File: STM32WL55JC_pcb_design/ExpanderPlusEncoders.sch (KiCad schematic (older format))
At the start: 8 parts

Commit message: Update ADC section to work with MAX11635
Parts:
- removed J? (x4): Conn_01x10_Male, Connector_JST:JST_GH_BM10B-GHS-TBT_1x10-1MP_P1.25mm_Vertical, symbol Connector:Conn_01x10_Male
- removed R?: 4k7, symbol Device:R_US
- added J? (x4): Conn_01x10, Connector_JST:JST_GH_BM10B-GHS-TBT_1x10-1MP_P1.25mm_Vertical, symbol Connector_Generic:Conn_01x10
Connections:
- wire segments 50 -> 46
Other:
- moved on the sheet: SW?
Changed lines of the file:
@@
 $Descr A4 11693 8268
 encoding utf-8
-Sheet 5 6
+Sheet 2 6
 Title ""
 Date ""
@@
 Wire Wire Line
 	2850 3300 2950 3300
-$Comp
-L Connector:Conn_01x10_Male J?
-U 1 1 6179BFE6
-P 2650 2900
-AR Path="/6179BFE6" Ref="J?"  Part="1"
-AR Path="/61789BD1/6179BFE6" Ref="J?"  Part="1"
-F 0 "J?" H 2758 3481 50  0000 C CNN
-F 1 "Conn_01x10_Male" H 2758 3390 50  0000 C CNN
-F 2 "Connector_JST:JST_GH_BM10B-GHS-TBT_1x10-1MP_P1.25mm_Vertical" H 2650 2900 50  0001 C CNN
-F 3 "~" H 2650 2900 50  0001 C CNN
-	1    2650 2900
-	1    0    0    -1
-$EndComp
 Text GLabel 2950 2500 2    50   Input ~ 0
 ENC1_1
@@
 Wire Wire Line
 	3800 3300 3900 3300
-$Comp
-L Connector:Conn_01x10_Male J?
-U 1 1 6179C000
-P 3600 2900
-AR Path="/6179C000" Ref="J?"  Part="1"
-AR Path="/61789BD1/6179C000" Ref="J?"  Part="1"
-F 0 "J?" H 3708 3481 50  0000 C CNN
-F 1 "Conn_01x10_Male" H 3708 3390 50  0000 C CNN
-F 2 "Connector_JST:JST_GH_BM10B-GHS-TBT_1x10-1MP_P1.25mm_Vertical" H 3600 2900 50  0001 C CNN
-F 3 "~" H 3600 2900 50  0001 C CNN
-	1    3600 2900
-	1    0    0    -1
-$EndComp
 Text GLabel 3900 2500 2    50   Input ~ 0
 ENC3_1
@@
 Wire Wire Line
 	2850 4500 2950 4500
-$Comp
-L Connector:Conn_01x10_Male J?
-U 1 1 6179C019
-P 2650 4100
-AR Path="/6179C019" Ref="J?"  Part="1"
-AR Path="/61789BD1/6179C019" Ref="J?"  Part="1"
-F 0 "J?" H 2758 4681 50  0000 C CNN
-F 1 "Conn_01x10_Male" H 2758 4590 50  0000 C CNN
-F 2 "Connector_JST:JST_GH_BM10B-GHS-TBT_1x10-1MP_P1.25mm_Vertical" H 2650 4100 50  0001 C CNN
-F 3 "~" H 2650 4100 50  0001 C CNN
-	1    2650 4100
-	1    0    0    -1
-$EndComp
 Text GLabel 2950 3700 2    50   Input ~ 0
 ENC5_1
@@
 Wire Wire Line
 	3800 4500 3900 4500
-$Comp
-L Connector:Conn_01x10_Male J?
-U 1 1 6179C032
-P 3600 4100
-AR Path="/6179C032" Ref="J?"  Part="1"
-AR Path="/61789BD1/6179C032" Ref="J?"  Part="1"
-F 0 "J?" H 3708 4681 50  0000 C CNN
-F 1 "Conn_01x10_Male" H 3708 4590 50  0000 C CNN
-F 2 "Connector_JST:JST_GH_BM10B-GHS-TBT_1x10-1MP_P1.25mm_Vertical" H 3600 4100 50  0001 C CNN
-F 3 "~" H 3600 4100 50  0001 C CNN
-	1    3600 4100
-	1    0    0    -1
-$EndComp
 Text GLabel 3900 3700 2    50   Input ~ 0
 ENC7_1
@@
 Text HLabel 8500 2400 2    50   Input ~ 0
 EXP_VDD
-Wire Wire Line
-	8500 3700 8900 3700
 $Comp
 L Switch:SW_MEC_5E SW?
 U 1 1 617D8DFE
-P 9100 3800
-F 0 "SW?" H 9100 4185 50  0000 C CNN
-F 1 "SW_MEC_5E" H 9100 4094 50  0000 C CNN
-F 2 "" H 9100 4100 50  0001 C CNN
-F 3 "http://www.apem.com/int/index.php?controller=attachment&id_attachment=1371" H 9100 4100 50  0001 C CNN
-	1    9100 3800
+P 9300 3800
+F 0 "SW?" H 9300 4185 50  0000 C CNN
+F 1 "SW_MEC_5E" H 9300 4094 50  0000 C CNN
+F 2 "" H 9300 4100 50  0001 C CNN
+F 3 "http://www.apem.com/int/index.php?controller=attachment&id_attachment=1371" H 9300 4100 50  0001 C CNN
+	1    9300 3800
 	1    0    0    -1
 $EndComp
-Wire Wire Line
-	8900 3700 8900 3800
-Connection ~ 8900 3700
-Wire Wire Line
-	9300 3800 9300 3700
-Text HLabel 9350 3800 2    50   Input ~ 0
-EXP_GND
-Text HLabel 9250 4600 2    50   Input ~ 0
+Text HLabel 8500 4600 2    50   Input ~ 0
 EXP_INT
-$Comp
-L Device:R_US R?
-U 1 1 617DE762
-P 9050 4450
-F 0 "R?" H 9118 4496 50  0000 L CNN
-F 1 "4k7" H 9118 4405 50  0000 L CNN
-F 2 "" V 9090 4440 50  0001 C CNN
-F 3 "~" H 9050 4450 50  0001 C CNN
-	1    9050 4450
-	1    0    0    -1
-$EndComp
-Wire Wire Line
-	9050 4300 9050 4200
-Wire Wire Line
-	9050 4600 9250 4600
-Wire Wire Line
-	9050 4600 8500 4600
-Connection ~ 9050 4600
-Wire Wire Line
-	9050 4200 9100 4200
-Wire Wire Line
-	9300 3800 9350 3800
-Connection ~ 9300 3800
-Text HLabel 9100 4200 2    50   Input ~ 0
-EXP_VDD
 Text HLabel 2950 3300 2    50   Input ~ 0
 OR1
@@
 Text GLabel 5700 4200 0    50   Input ~ 0
 ENC_RST_4
+Text HLabel 9750 3700 2    50   Input ~ 0
+EXP_VDD
+Wire Wire Line
+	9500 3700 9750 3700
+Wire Wire Line
+	8500 3700 9100 3700
+Wire Wire Line
+	9100 3700 9100 3800
+Connection ~ 9100 3700
+Wire Wire Line
+	9500 3700 9500 3800
+Connection ~ 9500 3700
+$Comp
+L Connector_Generic:Conn_01x10 J?
+U 1 1 61681B58
+P 2650 3000
+F 0 "J?" H 2568 2275 50  0000 C CNN
+F 1 "Conn_01x10" H 2568 2366 50  0000 C CNN
+F 2 "Connector_JST:JST_GH_BM10B-GHS-TBT_1x10-1MP_P1.25mm_Vertical" H 2650 3000 50  0001 C CNN
+F 3 "~" H 2650 3000 50  0001 C CNN
+	1    2650 3000
+	-1   0    0    1
+$EndComp
+$Comp
+L Connector_Generic:Conn_01x10 J?
+U 1 1 6168626C
+P 3600 3000
+F 0 "J?" H 3518 2275 50  0000 C CNN
+F 1 "Conn_01x10" H 3518 2366 50  0000 C CNN
+F 2 "Connector_JST:JST_GH_BM10B-GHS-TBT_1x10-1MP_P1.25mm_Vertical" H 3600 3000 50  0001 C CNN
+F 3 "~" H 3600 3000 50  0001 C CNN
+	1    3600 3000
+	-1   0    0    1
+$EndComp
+$Comp
+L Connector_Generic:Conn_01x10 J?
+U 1 1 61686F2D
+P 2650 4200
+F 0 "J?" H 2568 3475 50  0000 C CNN
+F 1 "Conn_01x10" H 2568 3566 50  0000 C CNN
+F 2 "Connector_JST:JST_GH_BM10B-GHS-TBT_1x10-1MP_P1.25mm_Vertical" H 2650 4200 50  0001 C CNN
+F 3 "~" H 2650 4200 50  0001 C CNN
+	1    2650 4200
+	-1   0    0    1
+$EndComp
+$Comp
+L Connector_Generic:Conn_01x10 J?
+U 1 1 61688106
+P 3600 4200
+F 0 "J?" H 3518 3475 50  0000 C CNN
+F 1 "Conn_01x10" H 3518 3566 50  0000 C CNN
+F 2 "Connector_JST:JST_GH_BM10B-GHS-TBT_1x10-1MP_P1.25mm_Vertical" H 3600 4200 50  0001 C CNN
+F 3 "~" H 3600 4200 50  0001 C CNN
+	1    3600 4200
+	-1   0    0    1
+$EndComp
 $EndSCHEMATC

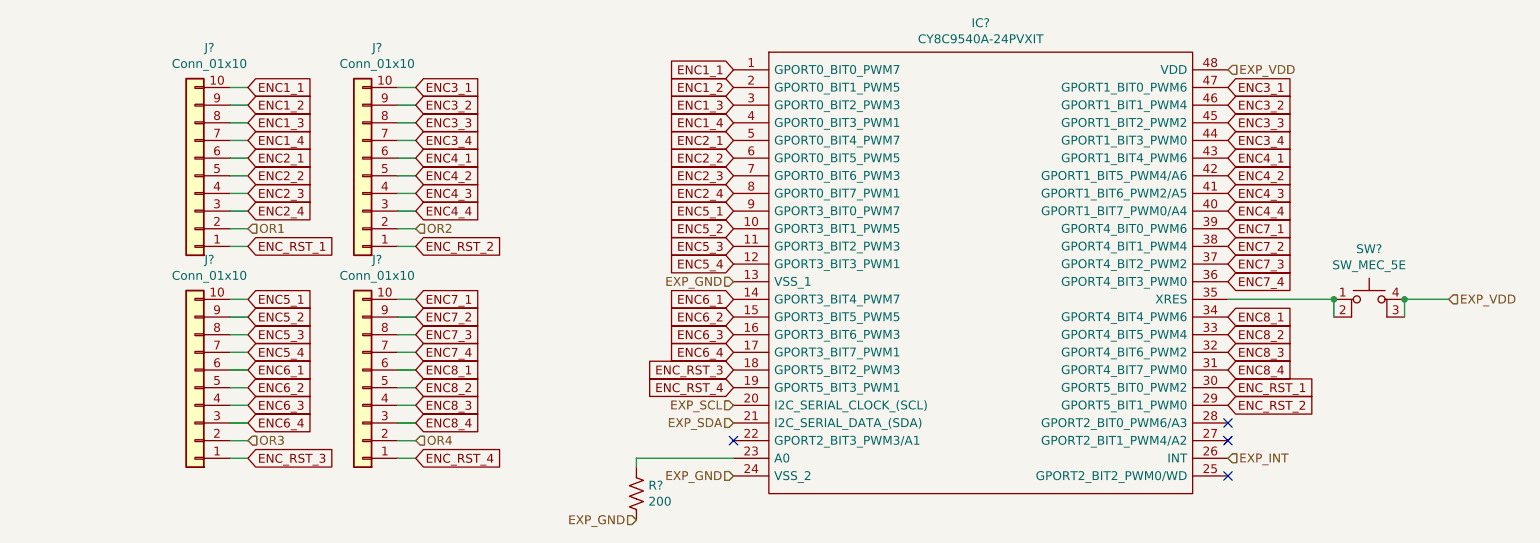
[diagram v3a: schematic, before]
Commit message: Finish component selection and footprint assignment
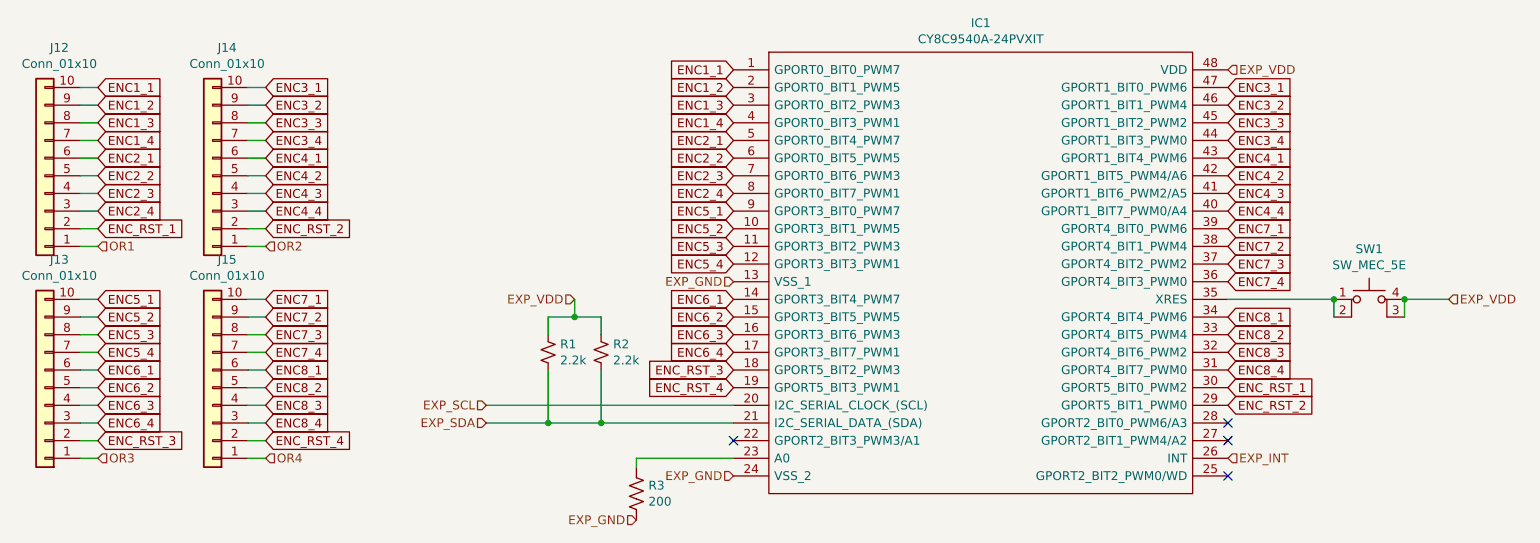
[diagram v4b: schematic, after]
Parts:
- added R1, R2: 2.2k, Resistor_SMD:R_0805_2012Metric, symbol Device:R_Small_US
- IC1: renamed from IC?; footprint SOP64P1035X279-48N -> CY8C9540A-24PVXIT:SOP64P1035X279-48N
- R3: renamed from R?; footprint (none) -> Resistor_SMD:R_0805_2012Metric
- SW1: renamed from SW?; footprint (none) -> EVQ-P2F02K:EVQP2V02W
- gave numbers to parts that had none: 4
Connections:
- net ENC_RST_1: now also J12.2 (Pin_2); no longer J12.1 (Pin_1)
- net ENC_RST_2: now also J14.2 (Pin_2); no longer J14.1 (Pin_1)
- net ENC_RST_3: now also J13.2 (Pin_2); no longer J13.1 (Pin_1)
- net ENC_RST_4: now also J15.2 (Pin_2); no longer J15.1 (Pin_1)
- net EXP_SDA: now also R1.2, R2.2
- net EXP_VDD: now also R1.1, R2.1
- net OR1: now also J12.1 (Pin_1); no longer J12.2 (Pin_2)
- net OR2: now also J14.1 (Pin_1); no longer J14.2 (Pin_2)
- net OR3: now also J13.1 (Pin_1); no longer J13.2 (Pin_2)
- net OR4: now also J15.1 (Pin_1); no longer J15.2 (Pin_2)
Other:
- moved on the sheet: J12, J13, J14, J15

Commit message: Initial pcb layout
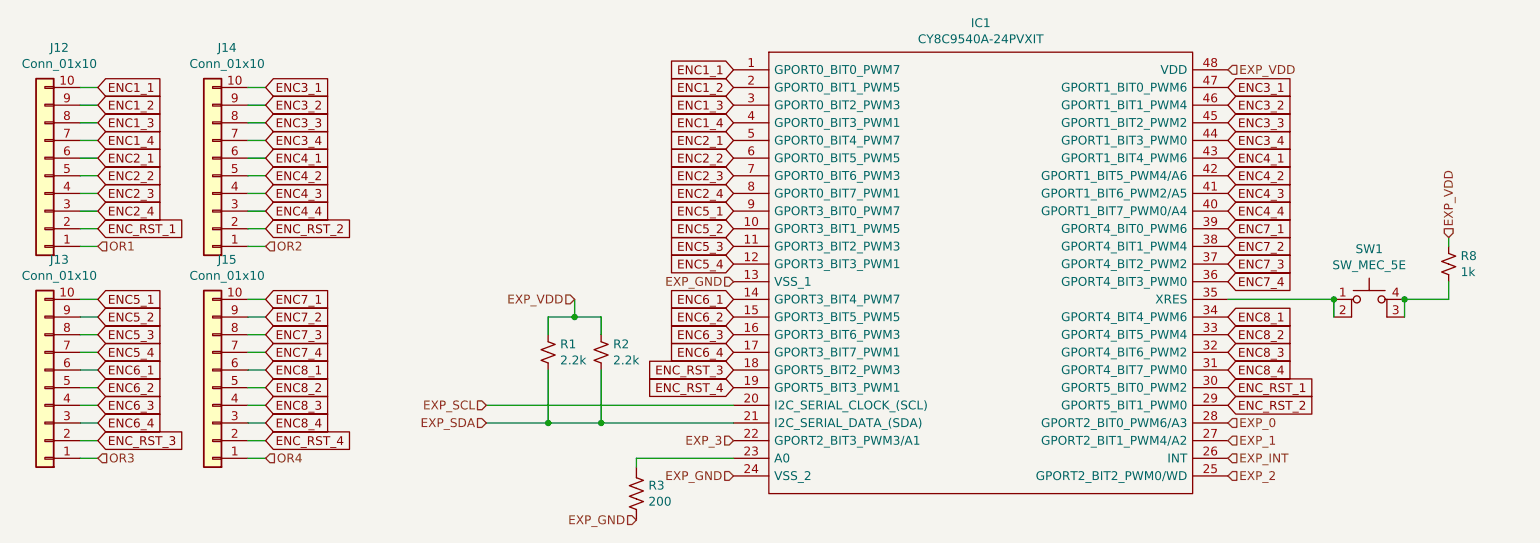
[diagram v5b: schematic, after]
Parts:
- added R8: 1k, Resistor_SMD:R_0805_2012Metric, symbol Device:R_Small_US
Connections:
- net EXP_VDD: now also R8.1; no longer SW1.3 (K), SW1.4 (A)
- net EXP_3: now reaches IC1.22 (GPORT2_BIT3_PWM3/A1)
- net EXP_2: now reaches IC1.25 (GPORT2_BIT2_PWM0/WD)
- net EXP_1: now reaches IC1.27 (GPORT2_BIT1_PWM4/A2)
- net EXP_0: now reaches IC1.28 (GPORT2_BIT0_PWM6/A3)
- new net: R8.2, SW1.3 (K), SW1.4 (A)
- no-connect marks 4 -> 0
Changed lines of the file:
@@
 Text HLabel 5150 4950 0    50   Input ~ 0
 EXP_GND
-NoConn ~ 5700 4500
-NoConn ~ 8500 4400
-NoConn ~ 8500 4500
-NoConn ~ 8500 4700
 Text GLabel 2100 3300 2    50   Input ~ 0
 ENC_RST_1
@@
 Text GLabel 5700 4200 0    50   Input ~ 0
 ENC_RST_4
-Text HLabel 9750 3700 2    50   Input ~ 0
+Text HLabel 9750 3350 1    50   Input ~ 0
 EXP_VDD
 Wire Wire Line
@@
 Text HLabel 4800 3700 0    50   Input ~ 0
 EXP_VDD
+$Comp
+L Device:R_Small_US R8
+U 1 1 615EB589
+P 9750 3500
+F 0 "R8" H 9818 3546 50  0000 L CNN
+F 1 "1k" H 9818 3455 50  0000 L CNN
+F 2 "Resistor_SMD:R_0805_2012Metric" H 9750 3500 50  0001 C CNN
+F 3 "~" H 9750 3500 50  0001 C CNN
+	1    9750 3500
+	1    0    0    -1
+$EndComp
+Wire Wire Line
+	9750 3600 9750 3700
+Wire Wire Line
+	9750 3400 9750 3350
+Text HLabel 5700 4500 0    50   Input ~ 0
+EXP_3
+Text HLabel 8500 4400 2    50   Input ~ 0
+EXP_0
+Text HLabel 8500 4500 2    50   Input ~ 0
+EXP_1
+Text HLabel 8500 4700 2    50   Input ~ 0
+EXP_2
 $EndSCHEMATC

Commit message: Finished component placement
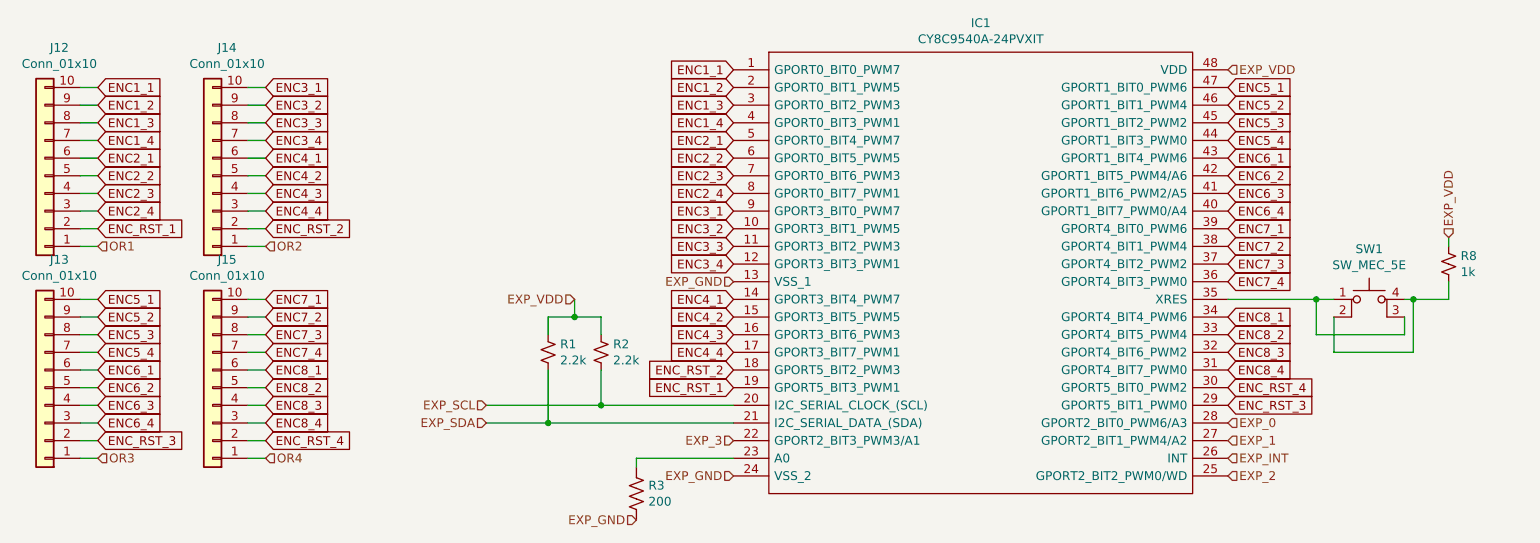
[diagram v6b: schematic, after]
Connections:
- net ENC3_1: now also IC1.9 (GPORT3_BIT0_PWM7); no longer IC1.47 (GPORT1_BIT0_PWM6)
- net ENC3_2: now also IC1.10 (GPORT3_BIT1_PWM5); no longer IC1.46 (GPORT1_BIT1_PWM4)
- net ENC3_3: now also IC1.11 (GPORT3_BIT2_PWM3); no longer IC1.45 (GPORT1_BIT2_PWM2)
- net ENC3_4: now also IC1.12 (GPORT3_BIT3_PWM1); no longer IC1.44 (GPORT1_BIT3_PWM0)
- net ENC4_1: now also IC1.14 (GPORT3_BIT4_PWM7); no longer IC1.43 (GPORT1_BIT4_PWM6)
- net ENC4_2: now also IC1.15 (GPORT3_BIT5_PWM5); no longer IC1.42 (GPORT1_BIT5_PWM4/A6)
- net ENC4_3: now also IC1.16 (GPORT3_BIT6_PWM3); no longer IC1.41 (GPORT1_BIT6_PWM2/A5)
- net ENC4_4: now also IC1.17 (GPORT3_BIT7_PWM1); no longer IC1.40 (GPORT1_BIT7_PWM0/A4)
- net ENC5_1: now also IC1.47 (GPORT1_BIT0_PWM6); no longer IC1.9 (GPORT3_BIT0_PWM7)
- net ENC5_2: now also IC1.46 (GPORT1_BIT1_PWM4); no longer IC1.10 (GPORT3_BIT1_PWM5)
- net ENC5_3: now also IC1.45 (GPORT1_BIT2_PWM2); no longer IC1.11 (GPORT3_BIT2_PWM3)
- net ENC5_4: now also IC1.44 (GPORT1_BIT3_PWM0); no longer IC1.12 (GPORT3_BIT3_PWM1)
- net ENC6_1: now also IC1.43 (GPORT1_BIT4_PWM6); no longer IC1.14 (GPORT3_BIT4_PWM7)
- net ENC6_2: now also IC1.42 (GPORT1_BIT5_PWM4/A6); no longer IC1.15 (GPORT3_BIT5_PWM5)
- net ENC6_3: now also IC1.41 (GPORT1_BIT6_PWM2/A5); no longer IC1.16 (GPORT3_BIT6_PWM3)
- net ENC6_4: now also IC1.40 (GPORT1_BIT7_PWM0/A4); no longer IC1.17 (GPORT3_BIT7_PWM1)
- net ENC_RST_1: now also IC1.19 (GPORT5_BIT3_PWM1); no longer IC1.30 (GPORT5_BIT0_PWM2)
- net ENC_RST_2: now also IC1.18 (GPORT5_BIT2_PWM3); no longer IC1.29 (GPORT5_BIT1_PWM0)
- net ENC_RST_3: now also IC1.29 (GPORT5_BIT1_PWM0); no longer IC1.18 (GPORT5_BIT2_PWM3)
- net ENC_RST_4: now also IC1.30 (GPORT5_BIT0_PWM2); no longer IC1.19 (GPORT5_BIT3_PWM1)
- net EXP_SCL: now also R2.2
- net EXP_SDA: no longer R2.2
- net at R8.2, SW1.4 (A): now also SW1.2; no longer SW1.3 (K)
- net at IC1.35 (XRES), SW1.1: now also SW1.3 (K); no longer SW1.2
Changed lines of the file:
@@
 	1    0    0    -1
 $EndComp
-Text GLabel 8500 2500 2    50   Input ~ 0
+Text GLabel 5700 3200 0    50   Input ~ 0
 ENC3_1
-Text GLabel 8500 2600 2    50   Input ~ 0
+Text GLabel 5700 3300 0    50   Input ~ 0
 ENC3_2
-Text GLabel 8500 2700 2    50   Input ~ 0
+Text GLabel 5700 3400 0    50   Input ~ 0
 ENC3_3
-Text GLabel 8500 2800 2    50   Input ~ 0
+Text GLabel 5700 3500 0    50   Input ~ 0
 ENC3_4
-Text GLabel 8500 2900 2    50   Input ~ 0
+Text GLabel 5700 3700 0    50   Input ~ 0
 ENC4_1
-Text GLabel 8500 3000 2    50   Input ~ 0
+Text GLabel 5700 3800 0    50   Input ~ 0
 ENC4_2
-Text GLabel 8500 3100 2    50   Input ~ 0
+Text GLabel 5700 3900 0    50   Input ~ 0
 ENC4_3
-Text GLabel 8500 3200 2    50   Input ~ 0
+Text GLabel 5700 4000 0    50   Input ~ 0
 ENC4_4
 Text GLabel 8500 3300 2    50   Input ~ 0
@@
 Text GLabel 5700 3100 0    50   Input ~ 0
 ENC2_4
-Text GLabel 5700 3200 0    50   Input ~ 0
+Text GLabel 8500 2500 2    50   Input ~ 0
 ENC5_1
-Text GLabel 5700 3300 0    50   Input ~ 0
+Text GLabel 8500 2600 2    50   Input ~ 0
 ENC5_2
-Text GLabel 5700 3400 0    50   Input ~ 0
+Text GLabel 8500 2700 2    50   Input ~ 0
 ENC5_3
-Text GLabel 5700 3500 0    50   Input ~ 0
+Text GLabel 8500 2800 2    50   Input ~ 0
 ENC5_4
-Text GLabel 5700 3700 0    50   Input ~ 0
+Text GLabel 8500 2900 2    50   Input ~ 0
 ENC6_1
-Text GLabel 5700 3800 0    50   Input ~ 0
+Text GLabel 8500 3000 2    50   Input ~ 0
 ENC6_2
-Text GLabel 5700 3900 0    50   Input ~ 0
+Text GLabel 8500 3100 2    50   Input ~ 0
 ENC6_3
-Text GLabel 5700 4000 0    50   Input ~ 0
+Text GLabel 8500 3200 2    50   Input ~ 0
 ENC6_4
 Text HLabel 4300 4300 0    50   Input ~ 0
@@
 Text GLabel 3050 4500 2    50   Input ~ 0
 ENC_RST_4
+Text GLabel 5700 4200 0    50   Input ~ 0
+ENC_RST_1
+Text GLabel 5700 4100 0    50   Input ~ 0
+ENC_RST_2
+Text GLabel 8500 4300 2    50   Input ~ 0
+ENC_RST_3
 Text GLabel 8500 4200 2    50   Input ~ 0
-ENC_RST_1
-Text GLabel 8500 4300 2    50   Input ~ 0
-ENC_RST_2
-Text GLabel 5700 4100 0    50   Input ~ 0
-ENC_RST_3
-Text GLabel 5700 4200 0    50   Input ~ 0
 ENC_RST_4
 Text HLabel 9750 3350 1    50   Input ~ 0
 EXP_VDD
 Wire Wire Line
-	9500 3700 9750 3700
-Wire Wire Line
-	8500 3700 9100 3700
-Wire Wire Line
-	9100 3700 9100 3800
-Connection ~ 9100 3700
-Wire Wire Line
-	9500 3700 9500 3800
-Connection ~ 9500 3700
+	9500 3700 9550 3700
+Wire Wire Line
+	8500 3700 9000 3700
 $Comp
 L Connector_Generic:Conn_01x10 J12
@@
 Wire Wire Line
 	4300 4400 4650 4400
-Wire Wire Line
-	4950 4400 4950 4100
-Connection ~ 4950 4400
 $Comp
 L Device:R_Small_US R2
@@
 $EndComp
 Wire Wire Line
-	4950 4400 5700 4400
-Wire Wire Line
 	4950 3900 4950 3800
 Wire Wire Line
@@
 Connection ~ 4650 4400
 Wire Wire Line
-	4650 4400 4950 4400
-Wire Wire Line
-	4300 4300 5700 4300
+	4300 4300 4950 4300
 Wire Wire Line
 	4800 3800 4800 3700
@@
 Text HLabel 8500 4700 2    50   Input ~ 0
 EXP_2
+Wire Wire Line
+	4650 4400 5700 4400
+Wire Wire Line
+	4950 4100 4950 4300
+Connection ~ 4950 4300
+Wire Wire Line
+	4950 4300 5700 4300
+Wire Wire Line
+	9000 3700 9000 3900
+Wire Wire Line
+	9000 3900 9500 3900
+Wire Wire Line
+	9500 3900 9500 3800
+Connection ~ 9000 3700
+Wire Wire Line
+	9000 3700 9100 3700
+Wire Wire Line
+	9100 3800 9100 4000
+Wire Wire Line
+	9100 4000 9550 4000
+Wire Wire Line
+	9550 4000 9550 3700
+Connection ~ 9550 3700
+Wire Wire Line
+	9550 3700 9750 3700
 $EndSCHEMATC

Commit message: Finish new design schematic
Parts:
- renumbered IC1 to IC2, R1 to R2, R2 to R3, R3 to R4, R8 to R5, SW1 to SW2
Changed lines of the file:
@@
 ENC8_4
 $Comp
-L CY8C9540A-24PVXIT:CY8C9540A-24PVXIT IC1
+L CY8C9540A-24PVXIT:CY8C9540A-24PVXIT IC2
 U 1 1 617A80A5
 P 5700 2400
-F 0 "IC1" H 7100 2665 50  0000 C CNN
+F 0 "IC2" H 7100 2665 50  0000 C CNN
 F 1 "CY8C9540A-24PVXIT" H 7100 2574 50  0000 C CNN
 F 2 "CY8C9540A-24PVXIT:SOP64P1035X279-48N" H 8350 2500 50  0001 L CNN
@@
 EXP_VDD
 $Comp
-L Switch:SW_MEC_5E SW1
+L Switch:SW_MEC_5E SW2
 U 1 1 617D8DFE
 P 9300 3800
-F 0 "SW1" H 9300 4185 50  0000 C CNN
+F 0 "SW2" H 9300 4185 50  0000 C CNN
 F 1 "SW_MEC_5E" H 9300 4094 50  0000 C CNN
 F 2 "EVQ-P2F02K:EVQP2V02W" H 9300 4100 50  0001 C CNN
@@
 	5150 4600 5150 4650
 $Comp
-L Device:R_US R3
+L Device:R_US R4
 U 1 1 617EA2B5
 P 5150 4800
-F 0 "R3" H 5218 4846 50  0000 L CNN
+F 0 "R4" H 5218 4846 50  0000 L CNN
 F 1 "200" H 5218 4755 50  0000 L CNN
 F 2 "Resistor_SMD:R_0805_2012Metric" V 5190 4790 50  0001 C CNN
@@
 $EndComp
 $Comp
-L Device:R_Small_US R1
+L Device:R_Small_US R2
 U 1 1 617B7086
 P 4650 4000
-F 0 "R1" H 4718 4046 50  0000 L CNN
+F 0 "R2" H 4718 4046 50  0000 L CNN
 F 1 "2.2k" H 4718 3955 50  0000 L CNN
 F 2 "Resistor_SMD:R_0805_2012Metric" H 4650 4000 50  0001 C CNN
@@
 	4300 4400 4650 4400
 $Comp
-L Device:R_Small_US R2
+L Device:R_Small_US R3
 U 1 1 617C398A
 P 4950 4000
-F 0 "R2" H 5018 4046 50  0000 L CNN
+F 0 "R3" H 5018 4046 50  0000 L CNN
 F 1 "2.2k" H 5018 3955 50  0000 L CNN
 F 2 "Resistor_SMD:R_0805_2012Metric" H 4950 4000 50  0001 C CNN
@@
 EXP_VDD
 $Comp
-L Device:R_Small_US R8
+L Device:R_Small_US R5
 U 1 1 615EB589
 P 9750 3500
-F 0 "R8" H 9818 3546 50  0000 L CNN
+F 0 "R5" H 9818 3546 50  0000 L CNN
 F 1 "1k" H 9818 3455 50  0000 L CNN
 F 2 "Resistor_SMD:R_0805_2012Metric" H 9750 3500 50  0001 C CNN
